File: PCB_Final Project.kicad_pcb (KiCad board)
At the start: 2 copper layers, 23 parts, among them J2 Conn_01x02_Pin, J4 Conn_01x02_Socket, K1 SANYOU_SRD_Form_C, Q1 BC547, U1 WeMos_D1_mini, U3 LM393

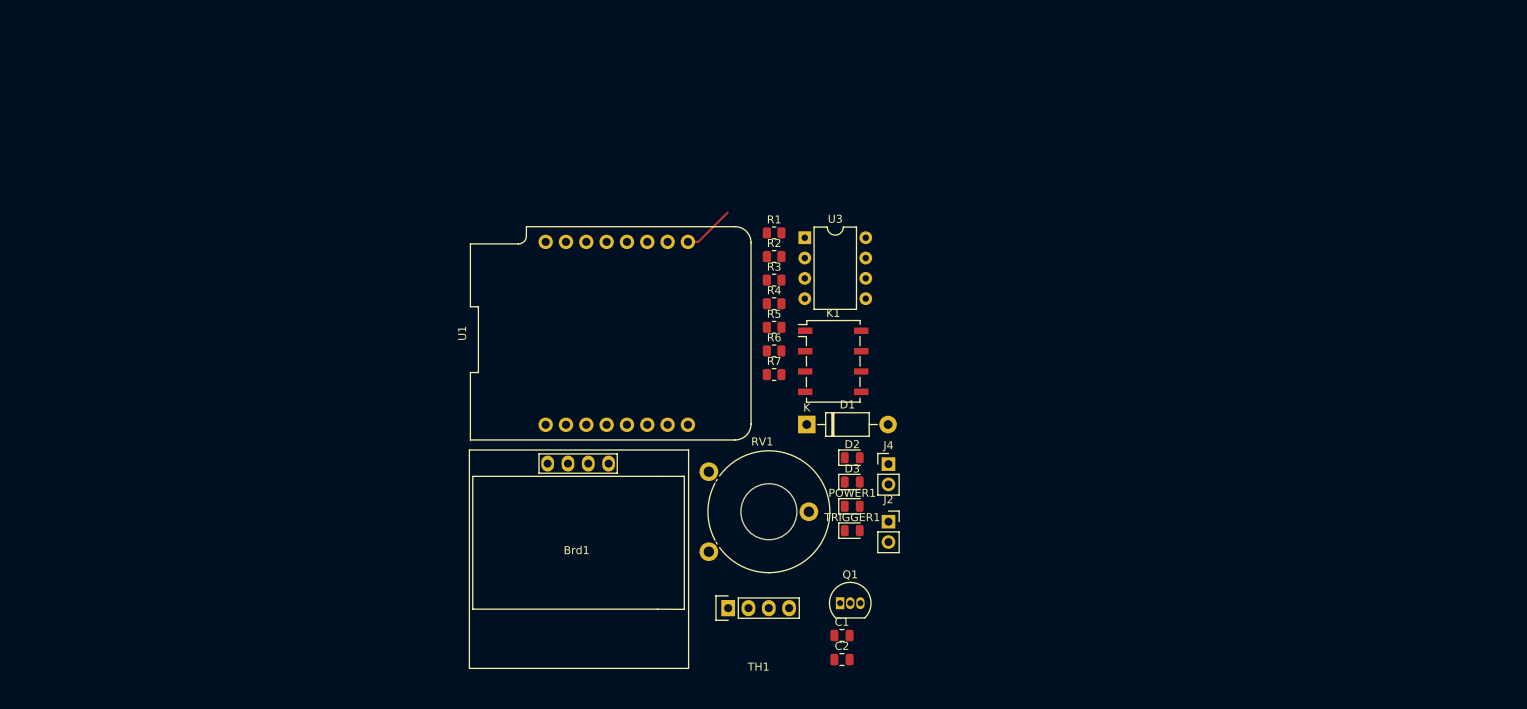
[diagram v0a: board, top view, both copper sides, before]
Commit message: update schematic
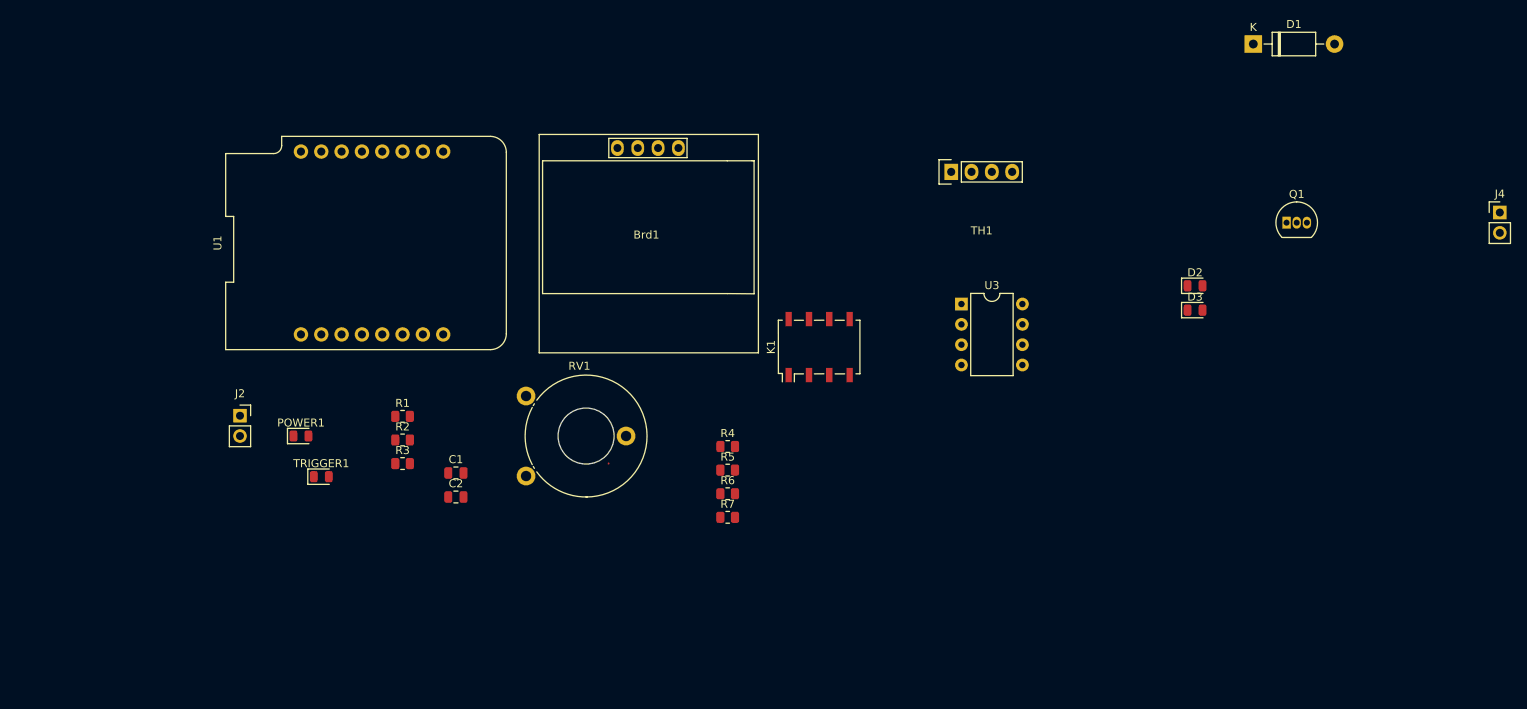
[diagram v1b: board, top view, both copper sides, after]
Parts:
- moved J4 82.6 mm to (215.9, 63.5)
- moved J2 82.1 mm to (58.4, 88.9)
- moved D1 73.3 mm to (185.1, 42.4)
- moved Q1 73.3 mm to (189.2, 64.8)
- moved POWER1 69.5 mm to (66.0, 91.4)
- moved TRIGGER1 66.7 mm to (68.6, 96.5)
- moved TH1 61.2 mm to (151.1, 58.4)
- moved C1 52.4 mm to (85.4, 96.0)
- moved C2 52.4 mm to (85.4, 99.1)
- moved R1 51.8 mm to (78.7, 89.0)
- moved R2 51.8 mm to (78.7, 91.9)
- moved R3 51.8 mm to (78.7, 94.9)
- moved D2 47.9 mm to (177.8, 72.7)
- moved D3 47.9 mm to (177.8, 75.7)
- moved Brd1 40.4 mm to (109.2, 66.0)
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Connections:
- U1 pad 13: /SDA -> /SCL
- U1 pad 14: /SCL -> /SDA
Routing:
- net unconnected-(U1-Rst-Pad1): track 6.49 -> 0.00 mm

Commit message: pcb done
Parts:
- removed C2: 104, Capacitor_SMD:C_0805_2012Metric
- removed J4: Conn_01x02_Socket, Connector_PinHeader_2.54mm:PinHeader_1x02_P2.54mm_Vertical
- removed RV1: R_Potentiometer, Potentiometer_THT:Potentiometer_Piher_PT-15-V02_Vertical_Hole
- removed TRIGGER1: LED, LED_SMD:LED_0805_2012Metric
- added D4: 1N4007, Diode_SMD:D_0805_2012Metric, F.Cu at (94.4, 95.7)
- added J1: Conn_01x02_Socket, Connector_Wire:SolderWire-2.5sqmm_1x02_P8.8mm_D2.4mm_OD4.4mm, F.Cu at (131.1, 110.2)
- added J3: Conn_01x02_Socket, Connector_Wire:SolderWire-2.5sqmm_1x02_P8.8mm_D2.4mm_OD4.4mm, F.Cu at (131.4, 89.5)
- added K2: Relay_SPDT, Relay_THT:Relay_SPDT_Finder_36.11, F.Cu at (105.8, 104.2)
- added Q2: NPN, Package_TO_SOT_SMD:TSOT-23, F.Cu at (100.3, 99.4)
- added REF**: MountingHole_3.2mm_M3, MountingHole:MountingHole_3.2mm_M3, F.Cu at (127.0, 61.0)
- added REF**: MountingHole_3.2mm_M3, MountingHole:MountingHole_3.2mm_M3, F.Cu at (33.0, 121.9)
- added REF**: MountingHole_3.2mm_M3, MountingHole:MountingHole_3.2mm_M3, F.Cu at (33.0, 61.0)
- added REF**: MountingHole_3.2mm_M3, MountingHole:MountingHole_3.2mm_M3, F.Cu at (127.0, 121.9)
- added U2: PC817, Package_DIP:DIP-4_W7.62mm_SMDSocket_SmallPads, F.Cu at (84.9, 81.1)
- C1: value 104 -> 0.1uF
- D1: footprint Diode_THT:D_DO-41_SOD81_P10.16mm_Horizontal -> Diode_SMD:D_0805_2012Metric
- K1: value SANYOU_SRD_Form_C -> Relay_SPDT; footprint Relay_SMD:Relay_DPDT_Omron_G6K-2F -> Relay_THT:Relay_SPDT_Finder_36.11
- Q1: value BC547 -> NPN; footprint Package_TO_SOT_THT:TO-92_Inline -> Package_TO_SOT_SMD:TSOT-23
- R2, R6: value 1k -> 330
- R3: value 1k -> 220
- U3: value LM393 -> PC817; footprint Package_DIP:DIP-8_W7.62mm -> Package_DIP:DIP-4_W7.62mm_SMDSocket_SmallPads
- moved D1 97.7 mm to (94.0, 77.6)
- moved D2 95.5 mm to (84.4, 92.7)
- moved D3 93.5 mm to (84.3, 74.7)
- moved Q1 90.6 mm to (100.1, 81.1)
- moved U3 68.1 mm to (84.9, 99.1)
- moved TH1 62.7 mm to (88.9, 66.3)
- moved Brd1 61.4 mm to (60.8, 103.8)
- moved C1 47.7 mm to (54.2, 59.9), turned to 180 degrees
- moved R3 46.9 mm to (54.2, 54.9), turned to 180 degrees
- moved R4 46.5 mm to (86.0, 60.4)
- moved POWER1 40.3 mm to (49.1, 54.9)
- moved R1 39.6 mm to (58.6, 54.9)
- moved R6 39.6 mm to (80.2, 92.6)
- moved J2 36.4 mm to (43.2, 55.9)
- moved R5 28.8 mm to (93.9, 82.2)
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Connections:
- D2 pad 1: Net-(D1-A) -> GND
- D3 pad 2: /IN -> Net-(D3-A)
- R2 pad 1: /3.3V -> /IN
- R5 pad 1: Net-(D2-A) -> Net-(R5-Pad1)
- R5 pad 2: /5V -> Net-(Q1-B)
- R6 pad 1: /5V -> /IN2
- R6 pad 2: /IN -> Net-(R6-Pad2)
- R7 pad 1: /IN -> Net-(R7-Pad1)
- R7 pad 2: Net-(Q1-B) -> Net-(Q2-B)
- U1 pad 11: unconnected-(U1-D4-Pad11) -> /IN2
- U3 pad 1: GND -> Net-(R6-Pad2)
- U3 pad 2: Net-(U3A--) -> Net-(D2-A)
- U3 pad 3: /ANALOG_MOISTURE -> Net-(R7-Pad1)
- U3 pad 4: (no net) -> /5V
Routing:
- net GND: track 0.00 -> 270.7 mm
- net /5V: track 0.00 -> 123.7 mm
- net /COM: track 0.00 -> 103.8 mm
- net /3.3V: track 0.00 -> 86.0 mm
- net /IN2: track 0.00 -> 50.8 mm
- net /NO: track 0.00 -> 45.9 mm
- net /ANALOG_MOISTURE: track 0.00 -> 41.7 mm
- net /DHT_DATA: track 0.00 -> 33.4 mm
- net /IN: track 0.00 -> 25.0 mm
- net Net-(D1-A): track 0.00 -> 17.5 mm
- net Net-(D4-A): track 0.00 -> 16.4 mm
- net Net-(D3-A): track 0.00 -> 9.42 mm
- net Net-(D2-A): track 0.00 -> 9.40 mm
- net /SDA: track 0.02 -> 5.58 mm
- net /SCL: track 0.02 -> 5.58 mm
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
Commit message: drc error correction
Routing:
- net /ANALOG_MOISTURE: track 41.7 -> 40.3 mm
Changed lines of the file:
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@@
   (segment (start 64.77 87.63) (end 64.77 93.206) (width 0.33) (layer "F.Cu") (net 1))
   (segment (start 62.23 87.63) (end 62.23 93.206) (width 0.33) (layer "F.Cu") (net 2))
-  (segment (start 57.15 93.206) (end 57.15 93.218) (width 1) (layer "F.Cu") (net 3))
   (segment (start 48.163 54.864) (end 48.163 58.577) (width 1) (layer "F.Cu") (net 3))
   (segment (start 57.15 93.206) (end 54.852 93.206) (width 1) (layer "F.Cu") (net 3))
@@
   (segment (start 88.7222 97.79) (end 88.7222 90.5002) (width 1) (layer "F.Cu") (net 4))
   (segment (start 57.658 60.96) (end 63.5 60.96) (width 0.33) (layer "F.Cu") (net 5))
-  (segment (start 60.452 53.895) (end 59.483 54.864) (width 0.33) (layer "F.Cu") (net 5))
   (segment (start 53.848 61.214) (end 55.118 59.944) (width 0.33) (layer "F.Cu") (net 5))
   (segment (start 67.31 64.77) (end 63.5 60.96) (width 0.33) (layer "F.Cu") (net 5))
@@
   (segment (start 60.706 51.816) (end 75.184 66.294) (width 1) (layer "F.Cu") (net 11))
   (segment (start 52.07 64.77) (end 43.942 64.77) (width 1) (layer "F.Cu") (net 11))
+  (segment (start 85.0684 66.2724) (end 85.09 66.294) (width 1) (layer "F.Cu") (net 11))
   (segment (start 40.132 60.96) (end 40.132 53.086) (width 1) (layer "F.Cu") (net 11))
   (segment (start 57.658 54.864) (end 55.118 54.864) (width 1) (layer "F.Cu") (net 11))
   (segment (start 54.61 51.816) (end 57.658 54.864) (width 1) (layer "F.Cu") (net 11))
-  (segment (start 85.09 66.294) (end 85.09 60.3974) (width 1) (layer "F.Cu") (net 11))
-  (segment (start 85.09 60.3974) (end 85.0684 60.3758) (width 1) (layer "F.Cu") (net 11))
-  (segment (start 75.184 66.294) (end 85.09 66.294) (width 1) (layer "F.Cu") (net 11))
-  (segment (start 85.09 60.6844) (end 85.3732 60.4012) (width 1) (layer "F.Cu") (net 11))
+  (segment (start 85.09 66.294) (end 75.184 66.294) (width 1) (layer "F.Cu") (net 11))
+  (segment (start 85.0684 60.3758) (end 85.0684 66.2724) (width 1) (layer "F.Cu") (net 11))
   (segment (start 54.61 51.816) (end 60.706 51.816) (width 1) (layer "F.Cu") (net 11))
   (segment (start 40.132 53.086) (end 41.402 51.816) (width 1) (layer "F.Cu") (net 11))
@@
   (segment (start 48.0314 88.5444) (end 56.1848 96.6978) (width 0.33) (layer "F.Cu") (net 30))
   (segment (start 57.15 87.63) (end 53.213 83.693) (width 0.33) (layer "F.Cu") (net 30))
-  (segment (start 81.1276 92.6338) (end 81.153 92.6592) (width 0.33) (layer "F.Cu") (net 31))
   (segment (start 81.1022 92.6592) (end 81.1022 97.79) (width 0.33) (layer "F.Cu") (net 31))
   (segment (start 81.1276 92.6338) (end 81.1022 92.6592) (width 0.33) (layer "F.Cu") (net 31))
